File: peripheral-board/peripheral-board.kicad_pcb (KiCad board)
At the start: 2 copper layers, 165 x 130 mm, 245 parts, among them CON1001 AVR-ISP-10, CON4001 BARREL_JACK, CON8001 SD_Card, J10001 DB15_FEMALE_HighDensity, J7001 FCR1295, P10001 VGA, P1001 Peripheral Bus, P1002 Power, Q4001 IRLML2244TRPbF, Q5001 IRLML2244TRPbF, Q5002 IRLML2244TRPbF, SW1001 Power, SW2001 1, SW2002 2, SW2003 3, SW2004 4, SW2005 5, SW2006 6, SW2007 7, SW2008 8, SW2009 9, SW2010 0, SW2011 +, SW2012 ´, SW2013 BKSP, SW2014 TROLL, SW2015 §, SW2016 UP, SW2017 RMB, SW2018 Q, SW2019 W, SW2020 E, SW2021 R, SW2022 T, SW2023 Y, SW2024 U, SW2025 I, SW2026 O, SW2027 P, SW2028 Å, SW2029 ¨, SW2030 RETURN, SW2031 ALT_GR, SW2032 <, SW2033 LEFT, SW2034 MMB, SW2035 A, SW2036 S, SW2037 D, SW2038 F, SW2039 G, SW2040 H, SW2041 J, SW2042 K, SW2043 L, SW2044 Ö, SW2045 Ä, SW2046 ', SW2047 ESC, SW2048 TAB, SW2049 ALT, SW2050 DOWN, SW2051 LMB, SW2052 SHIFT_L, SW2053 Z, SW2054 X, SW2055 C, SW2056 V, SW2057 B, SW2058 N, SW2059 M, SW2060 ,, SW2061 ., SW2062 -, SW2063 SHIFT_R, SW2064 FN_R, SW2065 SPACE, SW2066 FN_L, SW2067 RIGHT, SW2068 CTRL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

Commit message: routed spi
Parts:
- added C4004: 100u, Capacitors_Tantalum_SMD:TantalC_SizeD_EIA-7343_Reflow, B.Cu at (223.0, 44.0)
- added C4007: 100u, Capacitors_Tantalum_SMD:TantalC_SizeD_EIA-7343_Reflow, B.Cu at (201.4, 73.4)
- added C9001: 10u, Capacitors_SMD:C_1206, B.Cu at (246.5, 62.6)
- added D1001: LED_PWR, LEDs:LED-3MM, F.Cu at (73.1, 58.2)
- added D4003: SSL-LX3059IGW-CA, LEDs:LED-5MM-3, F.Cu at (64.2, 58.1)
- added D8001: LED_SD, LEDs:LED-3MM, F.Cu at (79.2, 71.9)
- added Q8001: BSS84LT1G, TO_SOT_Packages_SMD:SOT-23, B.Cu at (72.4, 73.0)
- added R1006: 1k, Resistors_SMD:R_0805, B.Cu at (74.0, 66.2)
- added R8003: 1k, Resistors_SMD:R_0805, B.Cu at (78.8, 79.7)
- added Y5001: 32768 Hz, Crystals:Crystal_Watch, F.Cu at (153.1, 161.7)
- L4001, L4002: footprint Choke_SMD:Choke_SMD_1206_Standard -> Choke_SMD:Choke_SMD_6.3x6.3_H3
- U1001, U5001: moved to F.Cu
- moved R8001 73.0 mm to (139.8, 113.2), turned to 270 degrees
- moved R8002 62.1 mm to (137.8, 113.2), turned to 270 degrees
- moved U5001 24.0 mm to (127.8, 144.0), turned to 90 degrees
- moved R1003 15.0 mm to (75.7, 120.2)
- moved R1004 14.8 mm to (73.8, 113.4)
- moved C4006 6.04 mm to (213.0, 68.0), turned to 180 degrees
- moved L4002 4.92 mm to (219.5, 73.0), turned to 270 degrees
- moved R4013 4.89 mm to (212.4, 74.4), turned to 0 degrees
- moved CON1001 4.65 mm to (100.6, 140.8)
- moved C4002 4.57 mm to (214.4, 53.4)
- moved C4008 4.37 mm to (210.7, 77.3), turned to 90 degrees
- moved U1001 3.02 mm to (99.6, 123.1), turned to 180 degrees
- moved C4009 2.47 mm to (212.8, 77.7), turned to 90 degrees
- moved L4001 2.01 mm to (219.1, 54.0)
- moved R4012 1.96 mm to (208.7, 77.1)
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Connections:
- C4006 pad 1: Net-(C4006-Pad1) -> VAA
- CONN9001 pad 18: /SPI_SCK -> /SPI_MOSI
- CONN9001 pad 19: /SPI_MOSI -> /SPI_SCK
- L4002 pad 1: Net-(C4006-Pad1) -> VAA
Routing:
- net /SPI_MISO: track 0.00 -> 198.2 mm
- net /SPI_SCK: track 0.00 -> 187.7 mm
- net /SPI_MOSI: track 0.00 -> 186.8 mm
- net /SPI_SS4: track 0.00 -> 183.9 mm
- net /SPI_SS5: track 0.00 -> 182.9 mm
- net /SPI_SS6: track 0.00 -> 182.0 mm
- net /SPI_SS7: track 0.00 -> 181.9 mm
- net /UART_RX: track 0.00 -> 173.7 mm
- net /EXTINT1: track 0.00 -> 173.5 mm
- net /UART_TX: track 0.00 -> 172.7 mm
- net /SPI_SS3: track 0.00 -> 36.9 mm

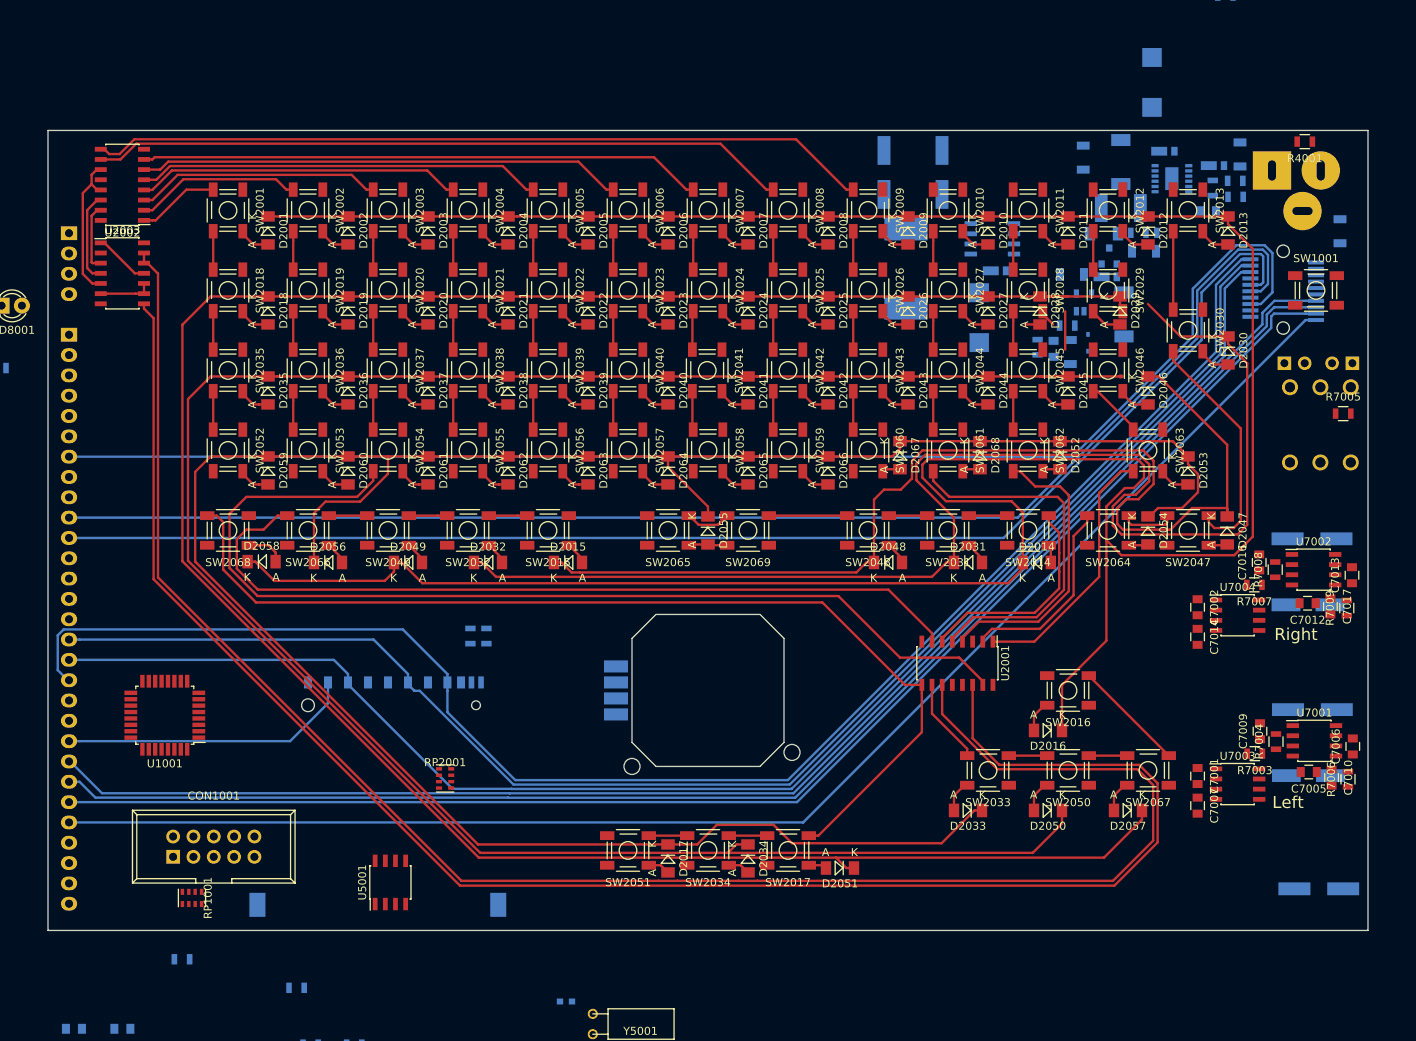
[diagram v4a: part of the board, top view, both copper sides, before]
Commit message: routed audio circuitry
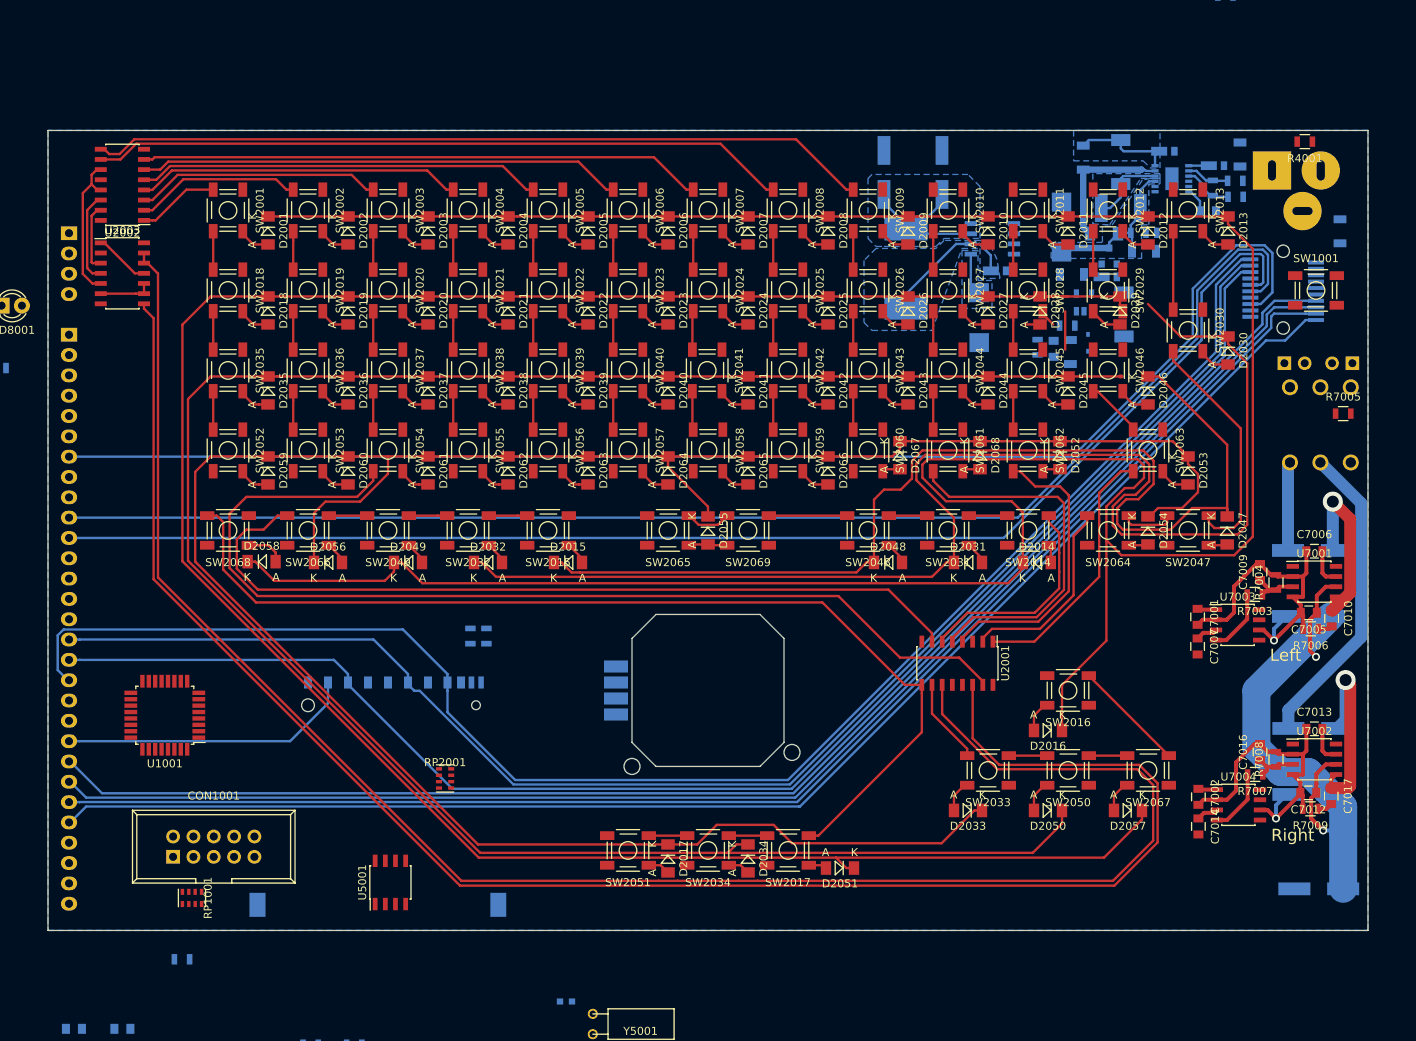
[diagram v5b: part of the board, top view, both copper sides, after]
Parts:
- removed R1005: R, Resistors_SMD:R_0805
- moved R7009 25.5 mm to (242.8, 134.8), turned to 180 degrees
- moved C7006 24.9 mm to (243.3, 102.6), turned to 0 degrees
- moved C7002 23.7 mm to (228.8, 133.3)
- moved C7012 23.7 mm to (242.6, 132.8)
- moved U7004 23.7 mm to (233.8, 134.3)
- moved C7003 23.7 mm to (242.6, 133.0)
- moved C7014 23.7 mm to (228.8, 137.0)
- moved C7015 23.7 mm to (243.1, 124.8), turned to 0 degrees
- moved C7016 23.7 mm to (236.5, 127.7)
- moved R7007 23.7 mm to (235.9, 130.5)
- moved C7017 23.7 mm to (245.4, 133.2)
- moved R7008 23.7 mm to (238.5, 128.6)
- moved U7002 23.7 mm to (243.3, 128.6)
- moved C4004 21.3 mm to (211.7, 62.1)
- moved C7007 19.9 mm to (228.7, 114.5)
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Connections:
- net Net-(C4002-Pad1) renamed /Power Supply/CHRG_SW
- net Net-(L4001-Pad2) renamed /Power Supply/CHRG_SENSE
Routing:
- net GND: track 0.00 -> 82.7 mm, vias 0 -> 2
- net VAA: track 0.00 -> 77.4 mm, vias 0 -> 2
- net /Audio/JACK_R: track 0.00 -> 39.1 mm
- net +3V3: track 0.00 -> 25.4 mm
- net Net-(C7015-Pad1): track 0.00 -> 24.4 mm, vias 0 -> 1
- net Net-(C7008-Pad1): track 0.00 -> 23.8 mm, vias 0 -> 1
- net +BATT: track 0.00 -> 20.6 mm
- net Net-(D4008-Pad1): track 0.00 -> 17.5 mm
- net Net-(C4002-Pad2): track 0.00 -> 17.4 mm
- net /Power Supply/CHRG_SW: track 0.00 -> 13.0 mm
- net /Audio/JACK_L: track 0.00 -> 11.1 mm
- net /Power Supply/CHRG_SENSE: track 0.00 -> 9.76 mm
- net Net-(R7003-Pad2): track 0.00 -> 8.07 mm
- net Net-(R7007-Pad2): track 0.00 -> 8.05 mm
- net Net-(R4006-Pad2): track 0.00 -> 6.26 mm
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- added copper zone on B.Cu, net +3V3
- added copper zone on B.Cu, net +BATT
- added copper zone on B.Cu, net /Power Supply/CHRG_SENSE
- added copper zone on B.Cu, net /Power Supply/CHRG_SW
- added copper zone on B.Cu, net GND
- added copper zone on B.Cu, net Net-(D4008-Pad1)
- added copper zone on B.Cu, net VAA

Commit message: added linear 3v3 reg for keyboard micro
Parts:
- added C1001: C, Capacitors_SMD:C_0805, F.Cu at (270.9, 122.9)
- added C1002: C, Capacitors_SMD:C_0805, F.Cu at (276.4, 122.9)
- added R1005: 100k, Resistors_SMD:R_0805, B.Cu at (57.7, 120.4)
- added U1002: L78L33ACUTR, TO_SOT_Packages_SMD:SOT89-3_Housing, F.Cu at (268.8, 128.3)
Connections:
- R1003 pad 1: Net-(R1003-Pad1) -> Net-(C1002-Pad1)
- R1004 pad 2: Net-(R1004-Pad2) -> GND
- SW1001 pad 1: Net-(SW1001-Pad1) -> GND
- U1001 pad 18: Net-(U1001-Pad18) -> Net-(C1002-Pad1)
- U1001 pad 4: Net-(U1001-Pad4) -> Net-(C1002-Pad1)

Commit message: routed traces.
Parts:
- removed CON1001: AVR-ISP-10, Connect:IDC_Header_Straight_10pins
- removed RP1001: 10k, Resistors_SMD:R_Cat16-4
- added R1007: 10k, Resistors_SMD:R_0805, F.Cu at (147.6, 170.1)
- added R1008: 47k, Resistors_SMD:R_0805, F.Cu at (125.8, 175.3)
- added R1009: 47k, Resistors_SMD:R_0805, F.Cu at (120.4, 175.3)
- added R1010: 47k, Resistors_SMD:R_0805, F.Cu at (114.9, 175.3)
- added TH5001: 10k, Capacitors_ThroughHole:CP_Radial_Tantal_D4.5mm_P2.50mm, F.Cu at (159.4, 24.6)
- C5001, C5002: value C_Small -> 22p
- C7007, C7014: footprint Capacitors_SMD:C_0805 -> Capacitors_SMD:C_1206
- D2001, D2002, D2003, D2004, D2005, D2006, D2007, D2008, D2009, D2010, D2011, D2012, D2013, D2014, D2015, D2016, D2017, D2018, D2019, D2020, D2021, D2022, D2023, D2024, D2025, D2026, D2027, D2028, D2029, D2030, D2031, D2032, D2033, D2034, D2035, D2036, D2037, D2038, D2039, D2040, D2041, D2042, D2043, D2044, D2045, D2046, D2047, D2048, D2049, D2050, D2051, D2052, D2053, D2054, D2055, D2056, D2057, D2058, D2059, D2060, D2061, D2062, D2063, D2064, D2065, D2066, D2067, D2068: footprint Diodes_SMD:MiniMELF_Standard -> Diodes_SMD:D_MiniMELF_Standard
- R1001, R1002: moved to F.Cu
- Y5001: moved to B.Cu
- moved C1002 206.4 mm to (70.1, 129.5)
- moved C1001 206.4 mm to (64.6, 129.5)
- moved U1002 206.4 mm to (62.5, 134.9)
- moved R1001 73.4 mm to (181.5, 127.7)
- moved R1002 68.0 mm to (182.7, 131.3)
- moved U5001 58.2 mm to (182.0, 122.7), turned to 270 degrees
- moved C5002 54.7 mm to (181.2, 120.1), turned to 90 degrees
- moved Y5001 53.1 mm to (182.5, 117.4), turned to 0 degrees
- moved C5001 51.6 mm to (183.8, 120.1), turned to 90 degrees
- moved U1001 47.5 mm to (147.0, 120.7), turned to 270 degrees
- moved RP2001 37.0 mm to (154.9, 100.0)
- moved D8001 14.5 mm to (74.4, 58.2), turned to 180 degrees
- moved D1001 14.2 mm to (58.9, 58.0)
- moved D2016 6.06 mm to (206.5, 120.0), turned to 270 degrees
- moved D2028 3.50 mm to (212.5, 72.5)
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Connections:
- C1002 pad 1: Net-(C1002-Pad1) -> +3.3VP
- CON8001 pad 9: Net-(CON8001-Pad9) -> RESET
- R1003 pad 1: Net-(C1002-Pad1) -> +3.3VP
- R1005 pad 2: Net-(C1002-Pad1) -> +3.3VP
- U1001 pad 18: Net-(C1002-Pad1) -> +3.3VP
- U1001 pad 19: /EXT_DET -> /AUD_CS_R
- U1001 pad 20: /PWR_BTN -> /AUD_UD
- U1001 pad 22: /EXT_AN -> /AUD_CS_L
- U1001 pad 23: /MOUSE_X -> /AUD_DET
- U1001 pad 24: /MOUSE_Y -> /PWR_BTN
- U1001 pad 25: /PWRON_RESET -> /EXT_DET
- U1001 pad 26: /CPURST -> /EXT_AN
- U1001 pad 29: /RESET -> RESET
- U1001 pad 30: /AUD_UD -> /MOUSE_X
- U1001 pad 31: /AUD_CS_L -> /MOUSE_Y
- U1001 pad 32: /AUD_CS_R -> /CPURST
- U1001 pad 4: Net-(C1002-Pad1) -> +3.3VP
- U1001 pad 7: /AUD_DET -> /PWRON_RESET
- U1002 pad 1: Net-(C1002-Pad1) -> +3.3VP
- U5001 pad 3: Net-(U5001-Pad3) -> +3.3VP
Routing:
- net /AUDIO_L: track 0.00 -> 232.6 mm, vias 0 -> 1
- net /AUDIO_R: track 0.00 -> 216.0 mm
- net /AUD_UD: track 0.00 -> 140.1 mm, vias 0 -> 2
- net /AUD_CS_R: track 0.00 -> 136.9 mm, vias 0 -> 2
- net +24V: track 0.00 -> 134.5 mm
- net /AUD_CS_L: track 0.00 -> 126.1 mm, vias 0 -> 2
- net /I2C_SDA: track 0.00 -> 125.1 mm, vias 0 -> 1
- net /I2C_SCL: track 0.00 -> 121.7 mm, vias 0 -> 1
- net +3V3: track 25.4 -> 129.2 mm
- net VAA: track 77.4 -> 102.2 mm
- net /KBD_Q2: track 399.3 -> 421.3 mm
- net /Keyboard/COL16: track 136.6 -> 152.7 mm
- net (no net): track 15.0 -> 0.00 mm
- net /KBD_Q1: track 464.3 -> 476.8 mm
- net /KBD_Q3: track 297.0 -> 308.5 mm
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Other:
- outline, holes or cut-outs redrawn
